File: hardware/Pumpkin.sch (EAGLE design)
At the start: 13 parts, among them Q1 BSS138

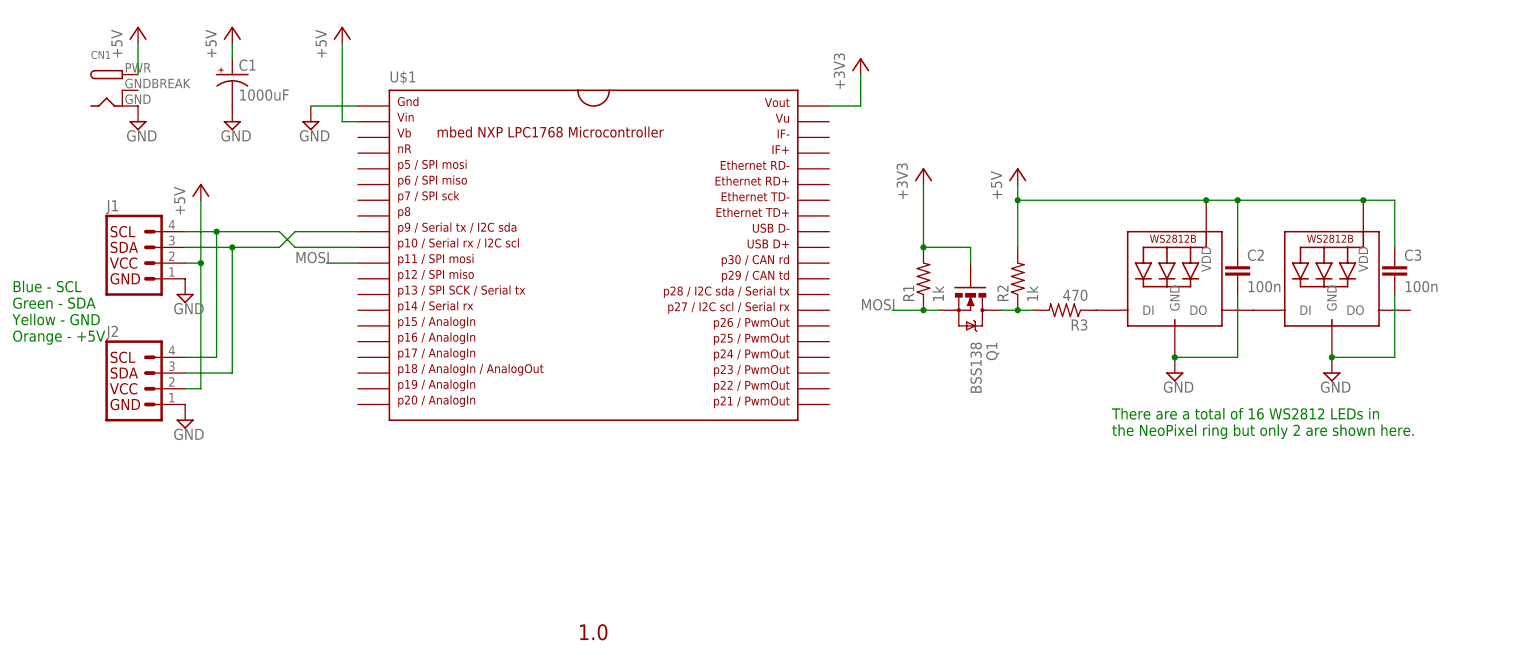
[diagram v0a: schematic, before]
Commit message: Fix I2C header
The Vcc and Gnd pins were swapped on the original schematic.
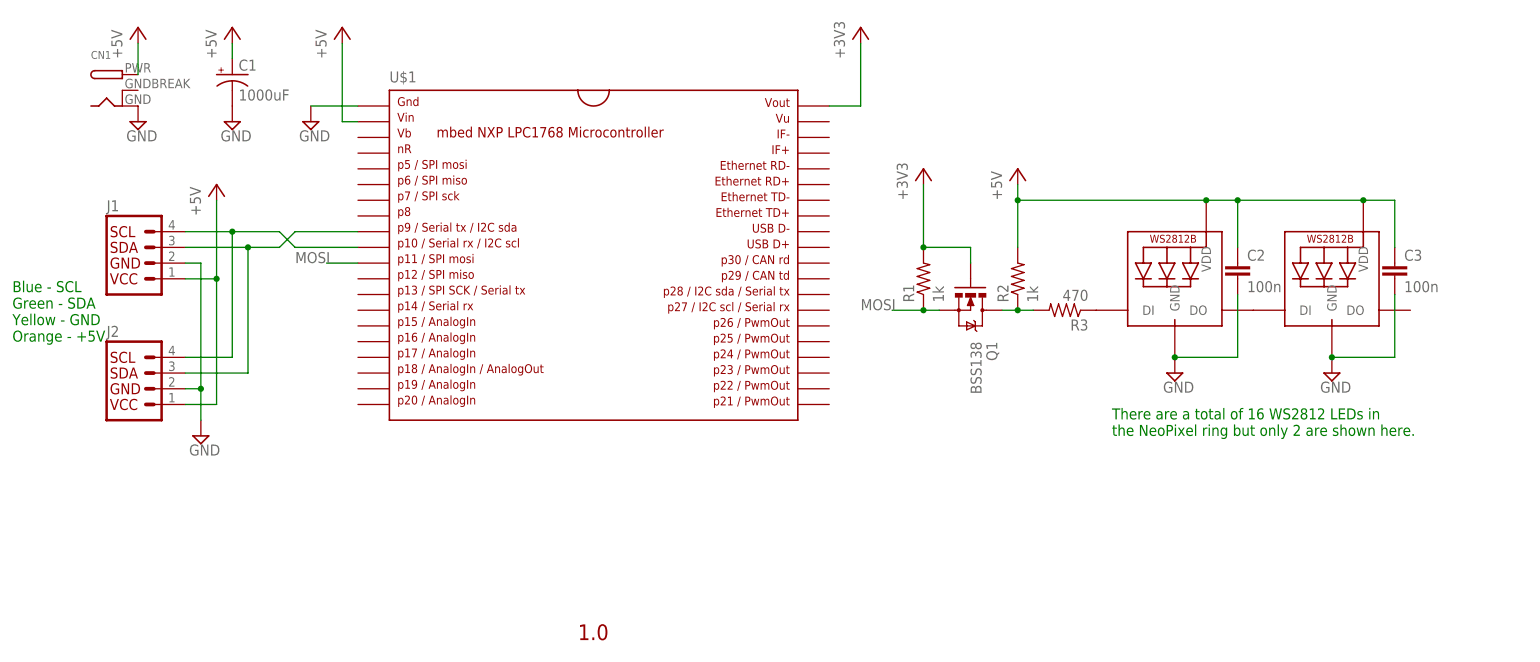
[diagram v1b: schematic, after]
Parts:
- J1, J2: device SparkFun-Connectors:I2C_STANDARD -> adam_custom:I2C_LEDEYES
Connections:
- net +5V: now also J1.1, J2.1; no longer J1.2, J2.2
- net GND: now also J1.2, J2.2; no longer J1.1, J2.1
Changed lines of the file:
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@@
 <part name="SUPPLY5" library="supply2" deviceset="GND" device=""/>
 <part name="P+4" library="supply1" deviceset="+5V" device=""/>
-<part name="J1" library="SparkFun-Connectors" deviceset="I2C_STANDARD" device=""/>
-<part name="SUPPLY6" library="supply2" deviceset="GND" device=""/>
+<part name="J1" library="adam_custom" deviceset="I2C_LEDEYES" device=""/>
 <part name="P+5" library="supply1" deviceset="+5V" device=""/>
-<part name="J2" library="SparkFun-Connectors" deviceset="I2C_STANDARD" device=""/>
+<part name="J2" library="adam_custom" deviceset="I2C_LEDEYES" device=""/>
 <part name="SUPPLY7" library="supply2" deviceset="GND" device=""/>
 </parts>
@@
 <instance part="U$1" gate="G$1" x="93.98" y="71.12"/>
 <instance part="SUPPLY1" gate="GND" x="48.26" y="91.44"/>
-<instance part="+3V1" gate="G$1" x="137.16" y="101.6"/>
+<instance part="+3V1" gate="G$1" x="137.16" y="106.68"/>
 <instance part="C1" gate="G$1" x="35.56" y="99.06"/>
 <instance part="SUPPLY2" gate="GND" x="35.56" y="91.44"/>
@@
 <instance part="P+4" gate="1" x="20.32" y="106.68"/>
 <instance part="J1" gate="G$1" x="17.78" y="63.5"/>
-<instance part="SUPPLY6" gate="GND" x="27.94" y="63.5"/>
-<instance part="P+5" gate="1" x="30.48" y="81.28"/>
+<instance part="P+5" gate="1" x="33.02" y="81.28"/>
 <instance part="J2" gate="G$1" x="17.78" y="43.18"/>
-<instance part="SUPPLY7" gate="GND" x="27.94" y="43.18"/>
+<instance part="SUPPLY7" gate="GND" x="30.48" y="40.64"/>
 </instances>
 <busses>
@@
 </segment>
 <segment>
-<pinref part="J1" gate="G$1" pin="1"/>
-<pinref part="SUPPLY6" gate="GND" pin="GND"/>
-</segment>
-<segment>
-<pinref part="J2" gate="G$1" pin="1"/>
+<pinref part="J2" gate="G$1" pin="2"/>
 <pinref part="SUPPLY7" gate="GND" pin="GND"/>
+<wire x1="27.94" y1="48.26" x2="30.48" y2="48.26" width="0.1524" layer="91"/>
+<wire x1="30.48" y1="48.26" x2="30.48" y2="43.18" width="0.1524" layer="91"/>
+<pinref part="J1" gate="G$1" pin="2"/>
+<wire x1="27.94" y1="68.58" x2="30.48" y2="68.58" width="0.1524" layer="91"/>
+<wire x1="30.48" y1="68.58" x2="30.48" y2="48.26" width="0.1524" layer="91"/>
+<junction x="30.48" y="48.26"/>
 </segment>
 </net>
@@
 <pinref part="+3V1" gate="G$1" pin="+3V3"/>
 <wire x1="132.08" y1="93.98" x2="137.16" y2="93.98" width="0.1524" layer="91"/>
-<wire x1="137.16" y1="93.98" x2="137.16" y2="99.06" width="0.1524" layer="91"/>
+<wire x1="137.16" y1="93.98" x2="137.16" y2="104.14" width="0.1524" layer="91"/>
 </segment>
 <segment>
@@
 </segment>
 <segment>
-<pinref part="J1" gate="G$1" pin="2"/>
+<pinref part="J1" gate="G$1" pin="1"/>
 <pinref part="P+5" gate="1" pin="+5V"/>
-<wire x1="27.94" y1="68.58" x2="30.48" y2="68.58" width="0.1524" layer="91"/>
-<wire x1="30.48" y1="68.58" x2="30.48" y2="78.74" width="0.1524" layer="91"/>
-<wire x1="30.48" y1="48.26" x2="30.48" y2="68.58" width="0.1524" layer="91"/>
-<junction x="30.48" y="68.58"/>
-<pinref part="J2" gate="G$1" pin="2"/>
-<wire x1="27.94" y1="48.26" x2="30.48" y2="48.26" width="0.1524" layer="91"/>
+<wire x1="27.94" y1="66.04" x2="33.02" y2="66.04" width="0.1524" layer="91"/>
+<wire x1="33.02" y1="66.04" x2="33.02" y2="78.74" width="0.1524" layer="91"/>
+<pinref part="J2" gate="G$1" pin="1"/>
+<wire x1="27.94" y1="45.72" x2="33.02" y2="45.72" width="0.1524" layer="91"/>
+<wire x1="33.02" y1="45.72" x2="33.02" y2="66.04" width="0.1524" layer="91"/>
+<junction x="33.02" y="66.04"/>
 </segment>
 </net>
@@
 </segment>
 </net>
-<net name="N$3" class="0">
-<segment>
+<net name="N$6" class="0">
+<segment>
+<pinref part="J2" gate="G$1" pin="3"/>
+<wire x1="27.94" y1="50.8" x2="38.1" y2="50.8" width="0.1524" layer="91"/>
+<pinref part="J1" gate="G$1" pin="3"/>
+<wire x1="27.94" y1="71.12" x2="38.1" y2="71.12" width="0.1524" layer="91"/>
+<wire x1="38.1" y1="71.12" x2="43.18" y2="71.12" width="0.1524" layer="91"/>
+<wire x1="43.18" y1="71.12" x2="45.72" y2="73.66" width="0.1524" layer="91"/>
+<pinref part="U$1" gate="G$1" pin="P$9"/>
+<wire x1="45.72" y1="73.66" x2="55.88" y2="73.66" width="0.1524" layer="91"/>
+<wire x1="38.1" y1="50.8" x2="38.1" y2="71.12" width="0.1524" layer="91"/>
+<junction x="38.1" y="71.12"/>
+</segment>
+</net>
+<net name="N$7" class="0">
+<segment>
+<pinref part="J2" gate="G$1" pin="4"/>
+<wire x1="27.94" y1="53.34" x2="35.56" y2="53.34" width="0.1524" layer="91"/>
 <pinref part="J1" gate="G$1" pin="4"/>
-<wire x1="27.94" y1="73.66" x2="33.02" y2="73.66" width="0.1524" layer="91"/>
-<wire x1="33.02" y1="73.66" x2="43.18" y2="73.66" width="0.1524" layer="91"/>
+<wire x1="27.94" y1="73.66" x2="35.56" y2="73.66" width="0.1524" layer="91"/>
+<wire x1="35.56" y1="73.66" x2="43.18" y2="73.66" width="0.1524" layer="91"/>
 <wire x1="43.18" y1="73.66" x2="45.72" y2="71.12" width="0.1524" layer="91"/>
 <pinref part="U$1" gate="G$1" pin="P$10"/>
 <wire x1="45.72" y1="71.12" x2="55.88" y2="71.12" width="0.1524" layer="91"/>
-<pinref part="J2" gate="G$1" pin="4"/>
-<wire x1="27.94" y1="53.34" x2="33.02" y2="53.34" width="0.1524" layer="91"/>
-<wire x1="33.02" y1="53.34" x2="33.02" y2="73.66" width="0.1524" layer="91"/>
-<junction x="33.02" y="73.66"/>
-</segment>
-</net>
-<net name="N$5" class="0">
-<segment>
-<pinref part="J1" gate="G$1" pin="3"/>
-<wire x1="27.94" y1="71.12" x2="35.56" y2="71.12" width="0.1524" layer="91"/>
-<wire x1="35.56" y1="71.12" x2="43.18" y2="71.12" width="0.1524" layer="91"/>
-<wire x1="43.18" y1="71.12" x2="45.72" y2="73.66" width="0.1524" layer="91"/>
-<pinref part="U$1" gate="G$1" pin="P$9"/>
-<wire x1="45.72" y1="73.66" x2="55.88" y2="73.66" width="0.1524" layer="91"/>
-<pinref part="J2" gate="G$1" pin="3"/>
-<wire x1="27.94" y1="50.8" x2="35.56" y2="50.8" width="0.1524" layer="91"/>
-<wire x1="35.56" y1="50.8" x2="35.56" y2="71.12" width="0.1524" layer="91"/>
-<junction x="35.56" y="71.12"/>
-</segment>
-</net>
+<wire x1="35.56" y1="53.34" x2="35.56" y2="73.66" width="0.1524" layer="91"/>
+<junction x="35.56" y="73.66"/>
+</segment>
+</net>
